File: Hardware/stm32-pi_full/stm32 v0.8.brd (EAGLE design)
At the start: 131.4 x 105.8 mm, 219 parts, among them J1 SOLDERJUMPERNO, Q1 MMBT3906, Q2 MMBT3904, Q3 MMBT3904, U1 ESP32-WROOM-32D

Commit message: update
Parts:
- added JP2, JP3: JUMPER-SMT_3_1-NC_TRACE_NO-SILK, SparkFun-Jumpers:SMT-JUMPER_3_1-NC_TRACE_NO-SILK
- R43: value 120k -> 120k 0.1%
- R53: value 10k -> 10k 0.1%
- RB9, RB9_: value 22r -> 22r 0.1%
- RF9, RV1: value 330R -> 330R 0.1%
- S1: value KSS221GLFS -> (none); device KSS221GLFS:KSS -> switch-omron:B3F-31XX
- moved RF1 97.8 mm to (114.6, 82.3)
- moved RF9 97.8 mm to (16.8, 84.6)
- moved RB1 97.6 mm to (117.5, 86.3), turned to 0 degrees
- moved RB9 97.6 mm to (20.0, 91.7), turned to 90 degrees
- moved RF2 72.4 mm to (101.7, 82.7)
- moved RF8 72.4 mm to (29.3, 84.6)
- moved RB2 71.5 mm to (104.2, 86.3), turned to 0 degrees
- moved RB8 71.5 mm to (32.9, 91.7), turned to 90 degrees
- moved RF3 47.1 mm to (89.5, 82.7)
- moved RF7 47.1 mm to (42.5, 86.2)
- moved RB3 46.6 mm to (91.9, 86.3), turned to 0 degrees
- moved RB7 46.6 mm to (45.6, 91.7), turned to 90 degrees
- moved RB4 25.6 mm to (84.0, 91.7)
- moved RB6 25.6 mm to (58.4, 91.7)
- moved RF4 24.7 mm to (79.6, 85.8)
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- renumbered RB10 to RB9_, RB11 to RB8_, RB12 to RB7_, RB13 to RB4_, RB14 to RB5_, RB15 to RB6_, RB16 to RB3_, RB17 to RB2_, RB18 to RB1_
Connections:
- removed net CT1_EX: EXPANSION.3, STM32F303VE.29
- removed net CT2_EX: EXPANSION.6, STM32F303VE.30
- removed net CT3_EX: EXPANSION.5, STM32F303VE.31
- removed net CT4_EX: EXPANSION.8, STM32F303VE.32
- removed net CT5_EX: EXPANSION.7, STM32F303VE.33
- removed net CT6_EX: EXPANSION.10, STM32F303VE.15
- removed net CT7_EX: EXPANSION.9, STM32F303VE.16
- new net CT_EX1: EXPANSION.3, STM32F303VE.23
- new net CT_EX2: EXPANSION.6, STM32F303VE.24
- new net CT_EX3: EXPANSION.5, STM32F303VE.15
- new net CT_EX4: EXPANSION.8, STM32F303VE.16
- new net CT_EX5: EXPANSION.7, STM32F303VE.17
- new net CT_EX6: EXPANSION.10, STM32F303VE.18
- new net PUSHIN_1_PRE: C1.1, D17.K, JP2.3, STM32F303VE.63
- new net PUSHIN_2_PRE: C19.1, D18.K, JP3.3, STM32F303VE.64
- net ADC_2_RJ45IN: now also STM32F303VE.61
- net BIAS: now also RB7.2, RB8.2, RB9.2; no longer RB1.2, RB2.2, RB3.2
- net CT1: now also CF9.2, STM32F303VE.35; no longer CF1.2, STM32F303VE.44
- net CT2: now also CF8.2, STM32F303VE.36; no longer CF2.2, STM32F303VE.43
- net CT3: now also CF7.2, STM32F303VE.38; no longer CF3.2, STM32F303VE.42
- net CT4: now also CF6.2, STM32F303VE.39; no longer CF4.2, STM32F303VE.41
- net CT6: now also CF4.2, STM32F303VE.41; no longer CF6.2, STM32F303VE.39
- net CT7: now also CF3.2, STM32F303VE.42; no longer CF7.2, STM32F303VE.38
- net CT8: now also CF2.2, STM32F303VE.43; no longer CF8.2, STM32F303VE.36
- net CT9: now also CF1.2, STM32F303VE.44; no longer CF9.2, STM32F303VE.35
- net GND: now also EXPANSION.9
- net N$10: now also RB7.1, RF7.1; no longer RB3.1, RF3.1
- net N$2: now also RB9.1, RF9.1; no longer RB1.1, RF1.1
- net N$26: now also RB1.2; no longer RB9.2
- net N$27: now also RB2.2; no longer RB8.2
- net N$28: now also RB3.2; no longer RB7.2
- net N$38: now also RB6.1, RF6.1; no longer RB4.1, RF4.1
- net N$40: now also RB4.1, RF4.1; no longer RB6.1, RF6.1
- net N$42: now also RB3.1, RF3.1; no longer RB7.1, RF7.1
- net N$43: now also RB2.1, RF2.1; no longer RB8.1, RF8.1
- net N$44: now also RB1.1, RF1.1; no longer RB9.1, RF9.1
- net N$8: now also RB8.1, RF8.1; no longer RB2.1, RF2.1
- net PULSE_2_RJ45: now also STM32F303VE.73
- net PUSHIN_1: now also JP2.2; no longer C1.1, D17.K, STM32F303VE.63
- net PUSHIN_2: now also JP3.2; no longer C19.1, D18.K, STM32F303VE.64
- net SCL: now also JP2.1
- net SDA: now also JP3.1
- net UART2_TX: no longer STM32F303VE.86
- net VSIG1: now also STM32F303VE.29; no longer STM32F303VE.23
- net VSIG2: now also STM32F303VE.30; no longer STM32F303VE.24
- net VSIG3: now also STM32F303VE.31; no longer STM32F303VE.27
- net VSIG4: now also STM32F303VE.32; no longer STM32F303VE.17
- net VSIG5: now also STM32F303VE.33; no longer STM32F303VE.18
- net VSIG6: now also STM32F303VE.34; no longer STM32F303VE.19
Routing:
- net ADC_2_RJ45IN: track 0.00 -> 96.2 mm, vias 0 -> 4
- net CT_EX4: track 0.00 -> 70.8 mm, vias 0 -> 2
- net CT4_EX: track 66.1 -> 0.00 mm, vias 2 -> 0
- net CT_EX5: track 0.00 -> 65.7 mm, vias 0 -> 2
- net CT5_EX: track 60.0 -> 0.00 mm, vias 2 -> 0
- net PUSHIN_2_PRE: track 0.00 -> 59.5 mm, vias 0 -> 2
- net PUSHIN_1_PRE: track 0.00 -> 57.8 mm, vias 0 -> 2
- net CT6_EX: track 57.4 -> 0.00 mm, vias 2 -> 0
- net PULSE_2_RJ45: track 6.66 -> 63.9 mm, vias 0 -> 2
- net PUSHIN_1: track 60.5 -> 4.06 mm, vias 2 -> 0
- net CT_EX6: track 0.00 -> 56.2 mm, vias 0 -> 2
- net PUSHIN_2: track 57.8 -> 4.15 mm, vias 2 -> 0
- net CT_EX2: track 0.00 -> 49.3 mm
- net CT2_EX: track 43.7 -> 0.00 mm, vias 2 -> 0
- net CT7_EX: track 41.8 -> 0.00 mm, vias 2 -> 0
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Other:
- board text added: "SCL"
- board text added: "SDA"
- board text added: "VCC"
- board text added: "v0.8"
- board text removed: "v0.7"

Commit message: commit
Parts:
- removed R6: 1.5k, rcl:R0603
- removed RV1: 330R 0.1%, resistor:R0603
- removed RV2, RV3: 330R, resistor:R0603
- removed TP5, TP6: TPB1,27, testpad:B1,27
- added C33: 47uF, rcl:C0805
- added IC1: AD8603UJ, analog-devices:SOT23-5
- added SJ22, SJ34, SJ35, SJ36, SJ37: SOLDERJUMPERNO, SparkFun:SJ_2S-NO
- added SVT1, SVT2, SVT3: SWS001, smd-special:SMS-001
- C12, C21: value 2.2uF -> 47uF
- CF1, CF2, CF3, CF4, CF5, CF6, CF7, CF8, CF9, CV1, CV2, CV3: value 100nF -> 10nF
- R21: value 200k -> 0R
- R43: value 120k 0.1% -> 120k
- R53: value 10k 0.1% -> 10k
- RB1, RB2, RB3, RB4, RB5, RB6, RB7, RB8, RB9: device rcl:R1206 -> rcl:R1210
- RF1, RF2, RF3, RF4, RF5, RF6, RF7, RF8: value 330R -> 9k1 0.1%
- RF9: value 330R 0.1% -> 9k1 0.1%
- moved R53 5.06 mm to (111.1, 46.7)
- moved CV2 5.01 mm to (110.7, 52.0)
- moved R41 4.12 mm to (115.5, 72.3)
- moved C23 3.47 mm to (83.9, 61.7)
- moved SJ15 3.41 mm to (64.6, 45.9)
- moved SJ17 3.21 mm to (65.4, 43.4)
- moved SJ16 3.19 mm to (66.3, 45.6)
- moved VREF_3V3 3.14 mm to (86.4, 62.2)
- moved R51 3.13 mm to (112.2, 74.4)
- moved CV3 2.94 mm to (111.1, 65.9)
- moved R52 2.85 mm to (112.1, 60.5)
- moved D3 2.80 mm to (112.6, 51.8), turned to 0 degrees
- moved R42 2.55 mm to (115.5, 58.4)
- moved D2 2.12 mm to (109.6, 43.1)
- moved CV1 1.80 mm to (108.9, 46.8)
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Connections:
- net SPI3_CS renamed SPI1_NSS
- removed net ADC0: R41.2, R51.1, RV3.1
- removed net D+: R6.2, STM32F303VE.71, TP5.TP, USB-C.A6
- removed net D-: STM32F303VE.70, TP6.TP, USB-C.A7
- removed net DIO0: PCB2.P$58, RFM69HCW.2, STM32F303VE.89, U1.24
- removed net IO11_EX: STM32F303VE.95
- removed net IO8_EX: STM32F303VE.91
- removed net N$34: R42.1, R52.1, RV2.1
- removed net N$37: R43.1, R53.1, RV1.1
- removed net SPI3_CLK: SJ15.1, STM32F303VE.78
- removed net SPI3_MISO: SJ16.1, STM32F303VE.79
- removed net SPI3_MOSI: SJ17.1, STM32F303VE.80
- new net DIO0_RFM: PCB2.P$58, RFM69HCW.2, STM32F303VE.88, U1.24
- new net N$18: STM32F303VE.80
- new net SPI1_CLK: SJ15.1, STM32F303VE.89
- new net SPI1_MISO: SJ16.1, STM32F303VE.90
- new net SPI1_MOSI: SJ17.1, STM32F303VE.91
- new net UART4_RX: SJ3.2, STM32F303VE.79
- new net UART4_TX: SJ18.2, STM32F303VE.78
- new net VREF+_: IC1.1, IC1.4, JP1.3, SJ2.2, STM32F303VE.21
- net +3V3: now also C33.1; no longer R6.1
- net +5V: now also IC1.5
- net AC1: now also SJ37.2, SVT1.2
- net AC2: now also SJ36.2, SVT2.2
- net AC3: now also SJ35.2, SVT3.2
- net GND: now also C33.2, IC1.2
- net IO1_EX: no longer STM32F303VE.97
- net MBUS_RX: now also SJ34.2
- net MBUS_TX: now also SJ22.2
- net PUSHIN_BYANT: now also STM32F303VE.97; no longer STM32F303VE.96
- net USART3_RX: now also SJ22.1, STM32F303VE.95; no longer SJ3.2, STM32F303VE.48
- net USART3_TX: now also SJ34.1, STM32F303VE.96; no longer SJ18.2, STM32F303VE.47
- net VREF+: now also IC1.3; no longer JP1.3, SJ2.2, STM32F303VE.21
- net VSIG1: now also R43.1, R53.1, SJ37.1, SVT1.1; no longer RV1.2
- net VSIG2: now also R42.1, R52.1, SJ36.1, SVT2.1; no longer RV2.2
- net VSIG3: now also R41.2, R51.1, SJ35.1, SVT3.1; no longer RV3.2
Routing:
- net DIO0_RFM: track 0.00 -> 136.9 mm, vias 0 -> 7
- net USART3_RX: track 145.4 -> 13.6 mm, vias 5 -> 0
- net DIO0: track 130.6 -> 0.00 mm, vias 7 -> 0
- net D+: track 117.4 -> 0.00 mm, vias 2 -> 0
- net D-: track 80.1 -> 0.00 mm, vias 4 -> 0
- net IO1_EX: track 57.8 -> 0.00 mm
- net VREF+_: track 0.00 -> 44.8 mm, vias 0 -> 4
- net VREF+: track 41.5 -> 3.51 mm, vias 4 -> 0
- net UART4_RX: track 0.00 -> 35.7 mm, vias 0 -> 4
- net USART3_TX: track 38.4 -> 12.1 mm, vias 5 -> 2
- net UART4_TX: track 0.00 -> 23.3 mm, vias 0 -> 3
- net VSIG2: track 66.3 -> 81.7 mm
- net VSIG3: track 58.3 -> 71.0 mm
- net VSIG1: track 73.2 -> 83.3 mm
- net +5V: track 324.4 -> 332.5 mm, vias 6 -> 4
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
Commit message: rPi_RFM additions
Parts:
- removed IC1: AD8603UJ, analog-devices:SOT23-5
- removed VREF_3V3: MCP1501T-33E, MCP1501T-33E:SOT95P280X145-6N
- added D14, D15, D16, D19, D20, D24, D25, D27, D28, D29, D30, D31, D32: ESD5Z3.3T1G, microbuilder:SOD-523
- added PS1: LT1461AIS8-3.3#PBF, LT1461AIS8:SOIC127P599X175-8N
- added R6: 0R, resistor:R0603
- added U$7: 47219-2001_MICROSD, MOLEX 47219-2001:47219-2001_MICROSD
- C23: value 200pF* -> 2.2uF; device rcl:C0603 -> rcl:C0805
- moved D1 52.5 mm to (7.93, 83.1), turned to 90 degrees
- moved SJ16 42.9 mm to (27.2, 28.0), flipped to the bottom, turned to 180 degrees
- moved SJ15 42.4 mm to (27.2, 25.8), flipped to the bottom, turned to 180 degrees
- moved SJ17 40.4 mm to (27.2, 30.1), flipped to the bottom, turned to 180 degrees
- moved SJ8 10.2 mm to (24.2, 47.8)
- moved SJ28 10.1 mm to (27.2, 32.3), flipped to the bottom
- moved C23 4.82 mm to (79.1, 61.1), turned to 270 degrees
- moved SJ14 2.50 mm to (24.2, 45.3), turned to 180 degrees
- moved SJ2 1.43 mm to (77.3, 62.8), turned to 90 degrees
- moved C17 1.21 mm to (78.2, 65.1)
- moved SJ1 0.67 mm to (93.6, 66.7)
- moved C11 0.58 mm to (83.9, 66.9)
- moved C13 0.33 mm to (79.6, 67.4)
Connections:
- removed net CS_STM32_RPI: PCB2.P$72, SJ8.1
- removed net RST_RFM_RPI: PCB2.P$69, SJ28.2
- removed net SCL_RPI: PCB2.P$68, SJ27.1
- removed net SDA_RPI: PCB2.P$67, SJ26.2
- removed net SPI1_CLK: SJ15.1, STM32F303VE.89
- removed net SPI1_MISO: SJ16.1, STM32F303VE.90
- removed net SPI1_MOSI: SJ17.1, STM32F303VE.91
- removed net VREF+_: IC1.1, IC1.4, JP1.3, SJ2.2, STM32F303VE.21
- new net BIAS_: R6.2, STM32F303VE.51
- new net N$11: PCB2.P$64, SJ8.1
- new net N$19: SJ8.2
- new net N$20: PCB2.P$43, SJ26.2
- new net N$21: PCB2.P$45, SJ27.1
- new net N$7: STM32F303VE.87
- new net SD_CLK: SJ17.1, U$7.PIN5
- new net SD_CS: SJ15.2, STM32F303VE.83
- new net SD_CS_: SJ15.1, U$7.PIN2
- new net SD_MISO: SJ28.1, U$7.PIN7
- new net SD_MOSI: SJ16.1, U$7.PIN3
- net +3V3: now also D1.K, D15.K, D16.K, D19.K, D20.K, D24.K, D25.K, D27.K, D28.K, D29.K, D30.A, D31.A, D32.A, SJ2.2, U$7.PIN4; no longer SJ2.1
- net +5V: now also PS1.2; no longer IC1.5, VREF_3V3.4, VREF_3V3.6
- net BIAS: now also D1.A, D14.K, R6.1; no longer D1.K, STM32F303VE.51
- net CS_RFM69: now also STM32F303VE.86; no longer PCB2.P$64
- net CS_STM32: no longer SJ14.1, SJ8.2
- net GND: now also D14.A, PS1.4, U$7.P$1, U$7.P$2, U$7.P$3, U$7.P$4, U$7.PIN6; no longer D1.A, IC1.2, VREF_3V3.2, VREF_3V3.3, VREF_3V3.5
- net MISO: now also SJ28.2, STM32F303VE.90; no longer SJ16.2
- net MOSI: now also SJ16.2, STM32F303VE.91; no longer SJ17.2
- net N$10: now also D19.A
- net N$13: now also SJ14.1
- net N$2: now also D15.A
- net N$38: now also D24.A
- net N$39: now also D20.A
- net N$40: now also D25.A
- net N$42: now also D27.A
- net N$43: now also D28.A
- net N$44: now also D29.A
- net N$8: now also D16.A
- net RST_RFM: now also STM32F303VE.85; no longer SJ28.1
- net SPI_CLK: now also SJ17.2, STM32F303VE.89; no longer SJ15.2
- net VREF+: now also JP1.3, PS1.6, SJ2.1, STM32F303VE.21; no longer IC1.3, VREF_3V3.1
- net VSIG1: now also D32.K
- net VSIG2: now also D31.K
- net VSIG3: now also D30.K
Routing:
- net CS_RFM69: track 146.3 -> 59.2 mm, vias 7 -> 4
- net DS18B20_2_RJ45: track 82.0 -> 6.26 mm, vias 4 -> 0
- net PUSHIN_3: track 77.8 -> 6.72 mm, vias 1 -> 0
- net PULSE_2_RJ45: track 63.9 -> 0.00 mm, vias 2 -> 0
- net CS_STM32: track 47.9 -> 0.00 mm, vias 3 -> 0
- net VREF+: track 3.51 -> 48.6 mm, vias 0 -> 4
- net VREF+_: track 44.8 -> 0.00 mm, vias 4 -> 0
- net RST_RFM: track 92.0 -> 58.8 mm, vias 9 -> 4
- net +3V3: track 91.2 -> 111.4 mm, vias 22 -> 37
- net SD_CS_: track 0.00 -> 9.35 mm
- net SD_MOSI: track 0.00 -> 9.00 mm
- net SD_CLK: track 0.00 -> 8.98 mm
- net SD_MISO: track 0.00 -> 8.97 mm
- net MOSI: track 91.4 -> 98.3 mm
- net SPI1_MOSI: track 6.23 -> 0.00 mm
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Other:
- board text added: "LT1461"
- board text removed: "MCP1501"

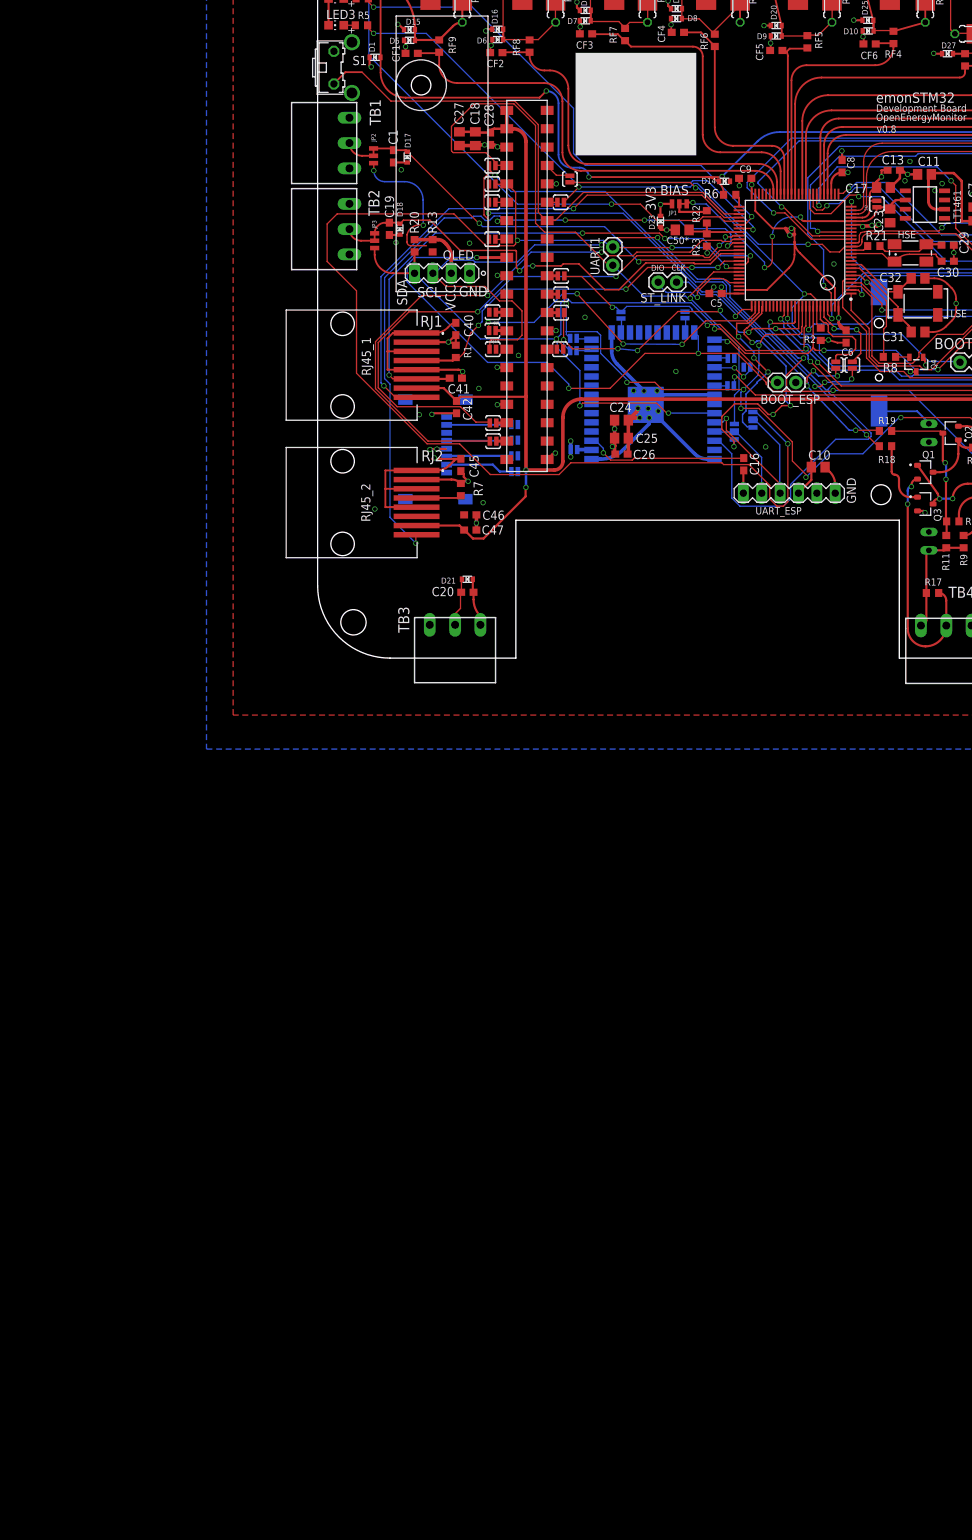
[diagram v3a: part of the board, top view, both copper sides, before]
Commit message: commit
RFM69
PULSE input
started on bringing in ds18b20 code from dBC's work.
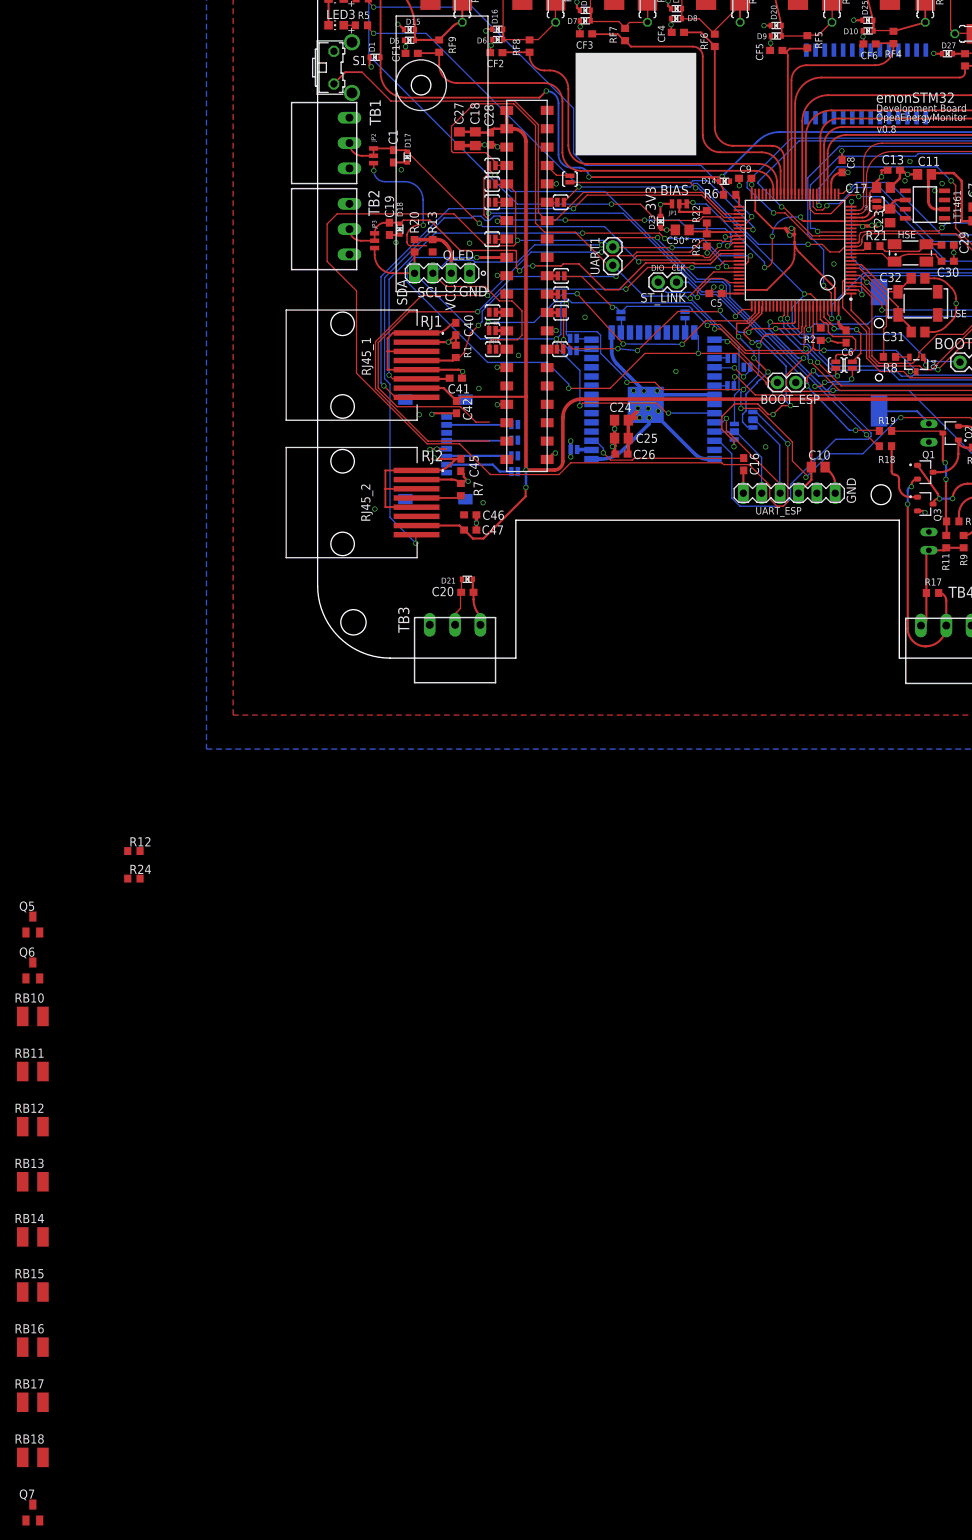
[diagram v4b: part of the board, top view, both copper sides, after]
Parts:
- removed SJ29, SJ30: SOLDERJUMPERNO, SparkFun:SJ_2S-NO
- added IC1: MCP23017T-E_SO, MCP23017T-E_SO:SOIC127P1030X265-28N
- added Q5, Q6, Q7: (no value), adafruit:SOT23
- added R12, R24: 0R, rcl:R0603
- added RB10: 22r 0.1%, rcl:R1210
- added RB11, RB12, RB13, RB14, RB15, RB16, RB17, RB18: 22r, rcl:R1210
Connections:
- removed net N$42: CT3.P$2, D11.K, D27.A, RB3.1, RB3_.1, RF3.1
- removed net N$43: CT2.P$2, D12.K, D28.A, RB2.1, RB2_.1, RF2.1
- removed net N$44: CT1.P$2, D13.K, D29.A, RB1.1, RB1_.1, RF1.1
- new net CT_IN1: CT1.P$2, D13.K, D29.A, Q5.3, RB1.1, RB1_.1, RF1.1
- new net CT_IN2: CT2.P$2, D12.K, D28.A, Q6.3, RB2.1, RB2_.1, RF2.1
- new net CT_IN3: CT3.P$2, D11.K, D27.A, Q7.3, RB3.1, RB3_.1, RF3.1
- new net GPB0: IC1.1, Q5.1
- new net GPB1: IC1.2, Q6.1
- new net GPB2: IC1.3, Q7.1
- new net MOS0: Q5.2, RB18.2
- new net MOS1: Q6.2, RB17.2
- new net MOS2: Q7.2, RB16.2
- new net N$37: RB15.2
- new net N$45: RB10.2
- new net N$46: RB11.2
- new net N$47: RB14.2
- new net N$48: RB13.2
- new net N$49: RB12.2
- net +3V3: now also IC1.9
- net BIAS: now also RB10.1, RB11.1, RB12.1, RB13.1, RB14.1, RB15.1, RB16.1, RB17.1, RB18.1
- net GND: now also IC1.10, IC1.15, IC1.16, IC1.17
- net NRST_STM: now also IC1.18
- net RPI_GPIO16: now also R12.2; no longer SJ29.2
- net RPI_GPIO16_RPI: now also R12.1; no longer SJ29.1
- net RPI_GPIO20: now also R24.2; no longer SJ30.2
- net RPI_GPIO20_RPI: now also R24.1; no longer SJ30.1
- net SCL: now also IC1.12
- net SDA: now also IC1.13
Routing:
- net N$44: track 19.8 -> 0.00 mm
- net CT_IN1: track 0.00 -> 19.8 mm
- net N$43: track 18.9 -> 0.00 mm
- net CT_IN2: track 0.00 -> 18.9 mm
- net N$42: track 18.4 -> 0.00 mm
- net CT_IN3: track 0.00 -> 18.4 mm
- net RPI_GPIO20_RPI: track 1.44 -> 0.01 mm
- net RPI_GPIO16_RPI: track 1.46 -> 0.05 mm
